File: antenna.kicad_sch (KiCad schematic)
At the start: 4 parts

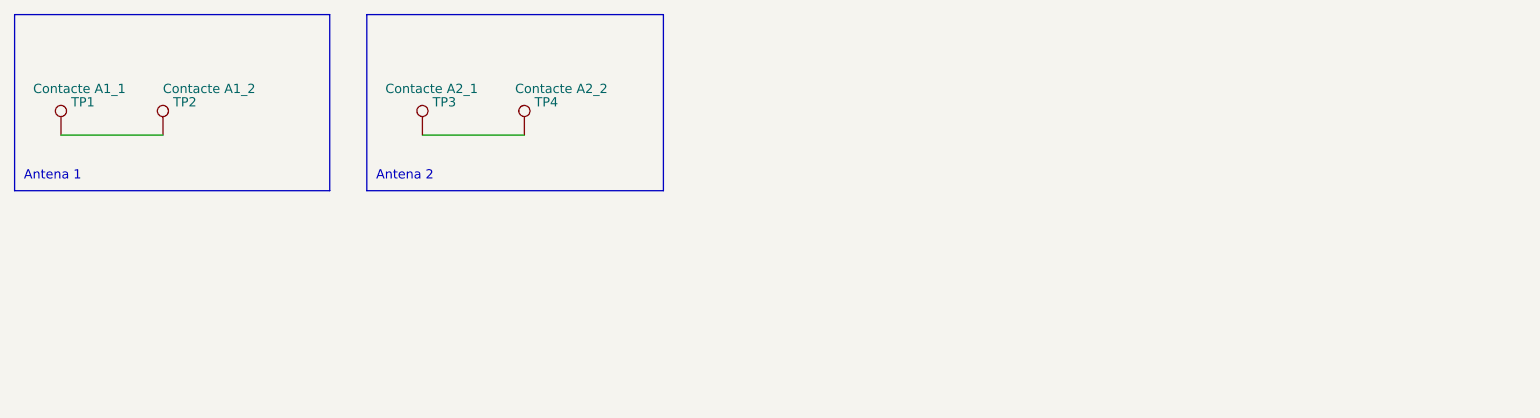
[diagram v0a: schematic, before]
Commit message: Afegit UFL, alineades bobines i aventades totes en sentit horari
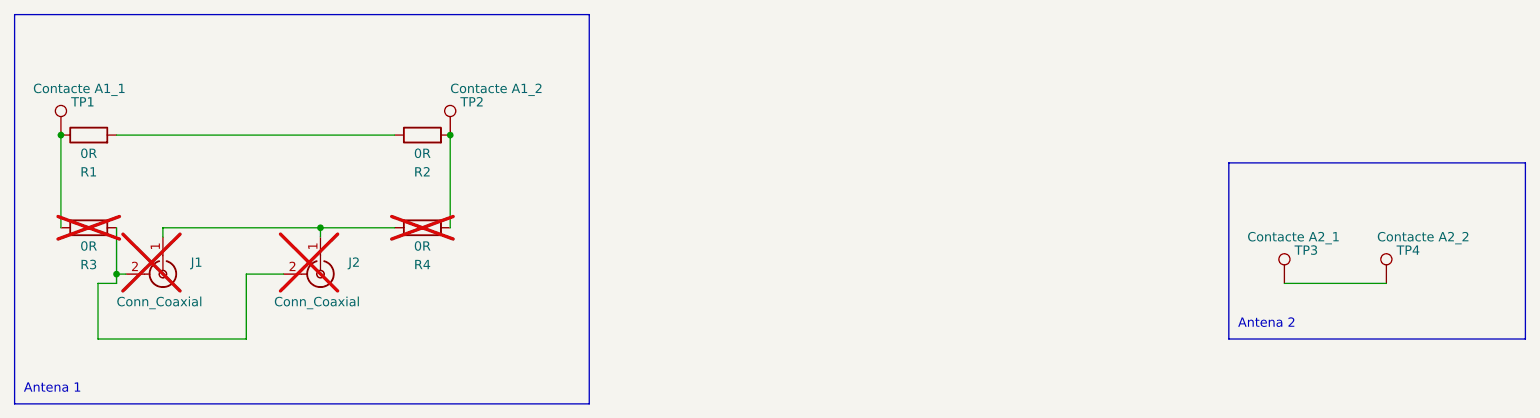
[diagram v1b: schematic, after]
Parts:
- added J1, J2: Conn_Coaxial, Library:U.FL-CON, symbol Connector:Conn_Coaxial
- added R1, R2: 0R, Jumper:SolderJumper-2_P1.3mm_Bridged_RoundedPad1.0x1.5mm, symbol Device:R
- added R3, R4: 0R, Jumper:SolderJumper-2_P1.3mm_Open_TrianglePad1.0x1.5mm, symbol Device:R
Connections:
- net at TP2.1: now also R2.2, R4.2; no longer TP1.1
- new net: J1.1 (In), J2.1 (In), R4.1
- new net: J1.2 (Ext), J2.2 (Ext), R3.2
- new net: R1.2, R2.1
- new net: R1.1, R3.1, TP1.1
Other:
- moved on the sheet: TP2, TP3, TP4

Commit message: Smaller details
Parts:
- removed R1: 0R, Jumper:SolderJumper-2_P1.3mm_Bridged_RoundedPad1.0x1.5mm, symbol Device:R
- removed R3: 0R, Jumper:SolderJumper-2_P1.3mm_Open_TrianglePad1.0x1.5mm, symbol Device:R
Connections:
- net at J1.2 (Ext), J2.2 (Ext): now also R2.1, TP1.1
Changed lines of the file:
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@@
 (kicad_sch (version 20230121) (generator eeschema)
   (paper "A4")
+  (junction (at 41.91 60.96) (diameter 0) (color 0 0 0 0)
+  )
+  (junction (at 87.63 41.91) (diameter 0) (color 0 0 0 0)
+  )
+  (junction (at 69.85 54.61) (diameter 0) (color 0 0 0 0)
+  )
   (junction (at 34.29 41.91) (diameter 0) (color 0 0 0 0)
   )
-  (junction (at 41.91 60.96) (diameter 0) (color 0 0 0 0)
-  )
-  (junction (at 87.63 41.91) (diameter 0) (color 0 0 0 0)
-  )
-  (junction (at 69.85 54.61) (diameter 0) (color 0 0 0 0)
-  )
   (wire (pts (xy 41.91 60.96) (xy 43.18 60.96))
     (stroke (width 0) (type default))
@@
     (stroke (width 0) (type default))
   )
-  (wire (pts (xy 41.91 41.91) (xy 80.01 41.91))
+  (wire (pts (xy 34.29 41.91) (xy 80.01 41.91))
     (stroke (width 0) (type default))
   )
@@
   )
   (wire (pts (xy 87.63 41.91) (xy 87.63 54.61))
+    (stroke (width 0) (type default))
+  )
+  (wire (pts (xy 34.29 54.61) (xy 41.91 54.61))
     (stroke (width 0) (type default))
   )
@@
         )
       )
-    )
-  )
-  (symbol (lib_id "Device:R") (at 38.1 54.61 90) (unit 1)
-    (in_bom yes) (on_board yes) (dnp yes)
-    (property "Reference" "R3" (at 38.1 59.69 90)
-      (effects (font (size 1.27 1.27)))
-    )
-    (property "Value" "0R" (at 38.1 57.15 90)
-      (effects (font (size 1.27 1.27)))
-    )
-    (property "Footprint" "Jumper:SolderJumper-2_P1.3mm_Open_TrianglePad1.0x1.5mm" (at 38.1 56.388 90)
-      (effects (font (size 1.27 1.27)) hide)
-    )
-    (property "Datasheet" "~" (at 38.1 54.61 0)
-      (effects (font (size 1.27 1.27)) hide)
-    )
-    (pin "2")
-    (pin "1")
-    (instances
-      (project "antenna"
-        (path "/f17842e6-4d37-4c6a-865b-0f19a9846610"
-          (reference "R3") (unit 1)
-        )
-      )
-    )
-  )
-  (symbol (lib_id "Device:R") (at 38.1 41.91 90) (unit 1)
-    (in_bom yes) (on_board yes) (dnp no)
-    (property "Reference" "R1" (at 38.1 46.99 90)
-      (effects (font (size 1.27 1.27)))
-    )
-    (property "Value" "0R" (at 38.1 44.45 90)
-      (effects (font (size 1.27 1.27)))
-    )
-    (property "Footprint" "Jumper:SolderJumper-2_P1.3mm_Bridged_RoundedPad1.0x1.5mm" (at 38.1 43.688 90)
-      (effects (font (size 1.27 1.27)) hide)
-    )
-    (property "Datasheet" "~" (at 38.1 41.91 0)
-      (effects (font (size 1.27 1.27)) hide)
-    )
-    (pin "2")
-    (pin "1")
-    (instances
-      (project "antenna"
-        (path "/f17842e6-4d37-4c6a-865b-0f19a9846610"
-          (reference "R1") (unit 1)
-        )
-      )
